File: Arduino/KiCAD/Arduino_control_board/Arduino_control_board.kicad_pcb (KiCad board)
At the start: 2 copper layers, 23 parts, among them J1 Buttons 0, J2 Buttons 1, SW1 SW_DPDT_x2, SW2 SW_DPDT_x2

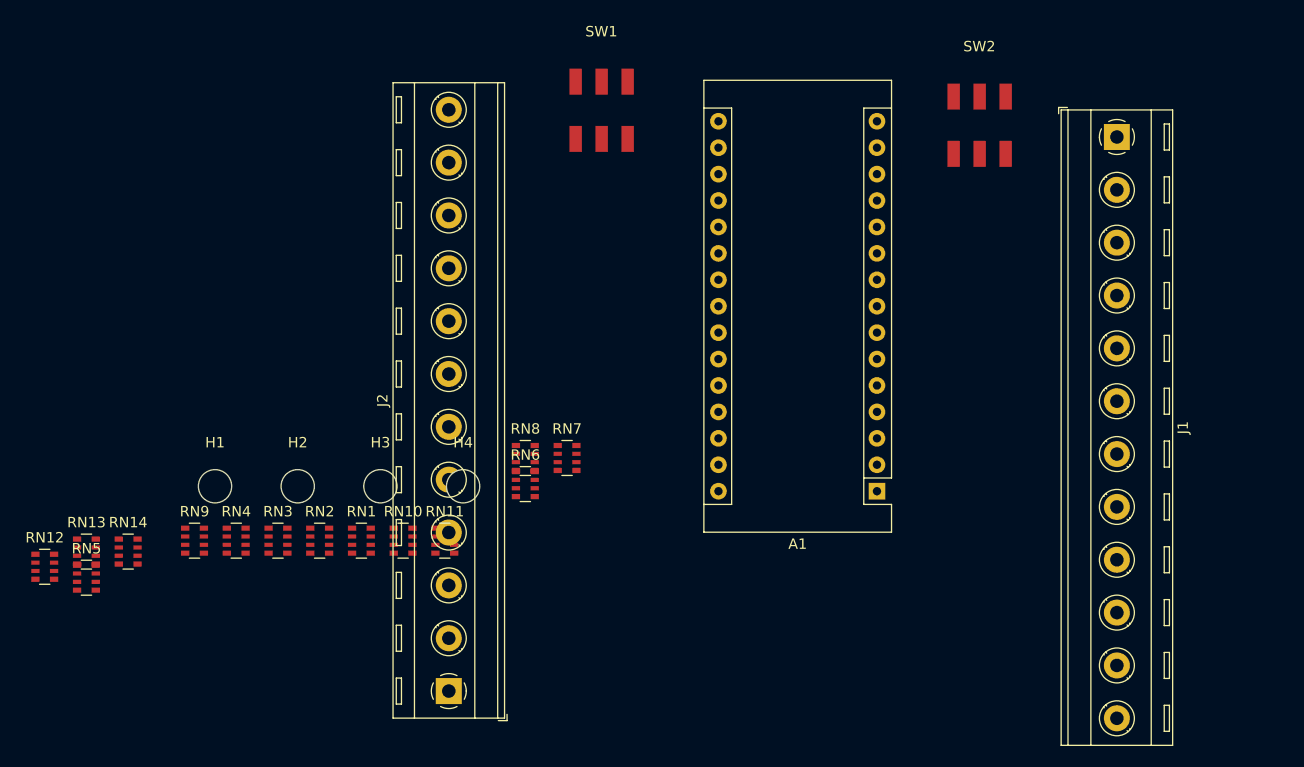
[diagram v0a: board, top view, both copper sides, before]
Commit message: 80% done with the controller. Will have done and ready for review this friday.
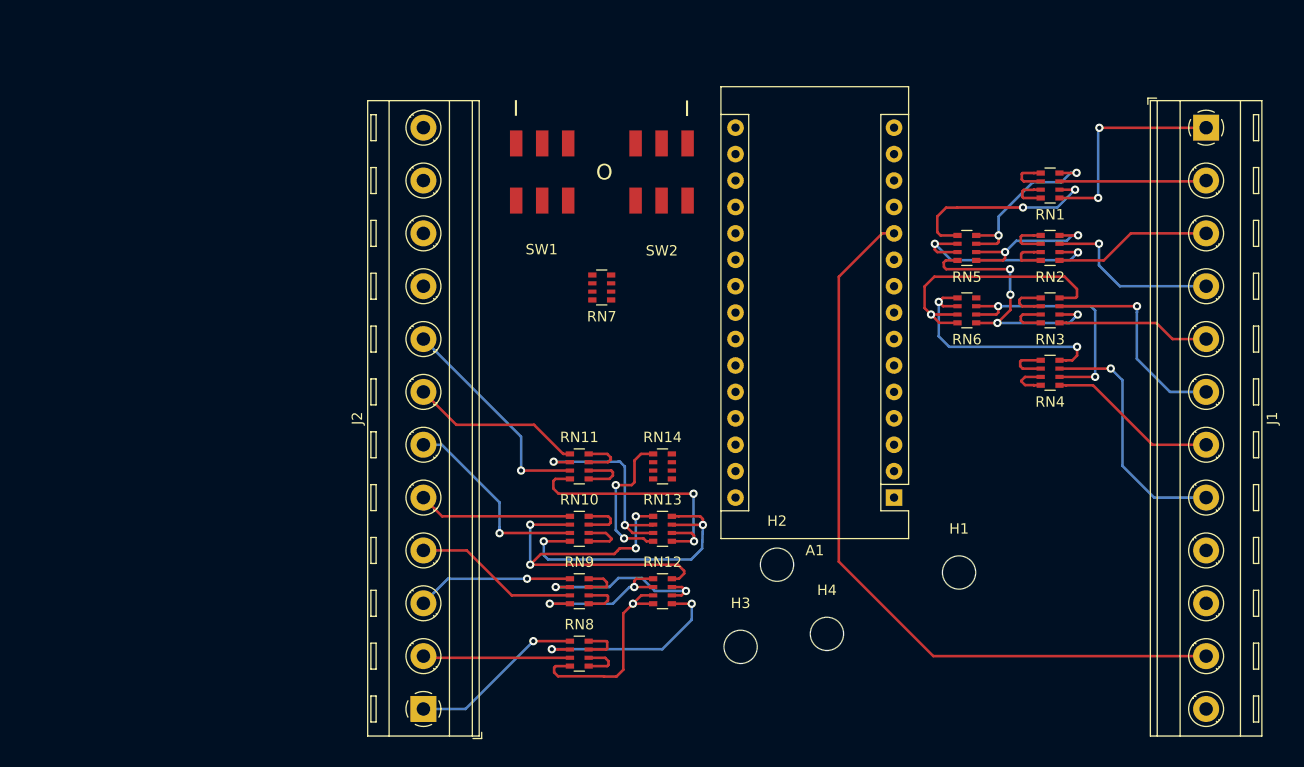
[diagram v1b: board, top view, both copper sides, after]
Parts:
- moved RN5 90.4 mm to (187.0, 51.0), turned to 180 degrees
- moved RN4 79.9 mm to (195.0, 63.0), turned to 180 degrees
- moved RN3 77.5 mm to (195.0, 57.0), turned to 180 degrees
- moved RN2 75.6 mm to (195.0, 51.0), turned to 180 degrees
- moved RN1 74.5 mm to (195.0, 45.0), turned to 180 degrees
- moved H1 72.0 mm to (186.2, 82.2)
- moved RN12 59.4 mm to (157.7, 84.0)
- moved RN13 55.4 mm to (157.7, 78.0)
- moved RN14 52.0 mm to (157.7, 72.0)
- moved H2 46.7 mm to (168.8, 81.5)
- moved RN6 45.6 mm to (187.0, 57.0), turned to 180 degrees
- moved H3 37.9 mm to (165.2, 89.3)
- moved H4 37.7 mm to (173.6, 88.1)
- moved RN9 37.3 mm to (149.7, 84.0)
- moved SW2 30.9 mm to (157.7, 43.7), turned to 180 degrees
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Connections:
- RN8 pad 3: B11 -> B10
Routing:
- net D_OUT_0: track 0.00 -> 73.5 mm
- net B13_O: track 0.00 -> 39.9 mm, vias 0 -> 4
- net B09_O: track 0.00 -> 39.2 mm, vias 0 -> 4
- net B14_O: track 0.00 -> 28.6 mm, vias 0 -> 2
- net B6_O: track 0.00 -> 26.4 mm, vias 0 -> 1
- net B5_O: track 0.00 -> 25.8 mm, vias 0 -> 4
- net B16_O: track 0.00 -> 25.6 mm, vias 0 -> 2
- net B7_O: track 0.00 -> 24.2 mm, vias 0 -> 2
- net B8: track 0.00 -> 24.1 mm, vias 0 -> 1
- net B8_O: track 0.00 -> 23.7 mm, vias 0 -> 2
- net B3_O: track 0.00 -> 21.5 mm, vias 0 -> 2
- net B16: track 0.00 -> 21.2 mm, vias 0 -> 1
- net B1: track 0.00 -> 20.8 mm, vias 0 -> 2
- net B6: track 0.00 -> 20.5 mm, vias 0 -> 1
- net B10_O: track 0.00 -> 20.1 mm, vias 0 -> 1
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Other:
- board text added: "I"
- board text added: "O"
